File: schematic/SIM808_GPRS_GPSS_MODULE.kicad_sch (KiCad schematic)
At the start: 37 parts, among them IC4 SIM7600G-H_R2, J10 SIM_Card_Shielded, Q1 BC817, Q15 SI2302, Q16 SI2302, Q2 BC817

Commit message: Routing
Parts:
- removed J10: SIM_Card_Shielded, MACHADA_footprints:NANO_SIM_SHELL_SMN305, symbol fridgeduino-rescue:SIM_Card_Shielded-Connector-gsm_lora_logger-rescue-gsm_lora_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
- added J1: SIM7155-6-1-14-A, SIM7155-6-1-14-A_GCT, symbol simHolderPush:SIM7155-6-1-14-A
- AE3, AE4: footprint greencharge-footprints:UFL_COAX_CONN23370191 -> antenna:CONN_2337019-1_TEC
- IC4: footprint SIM7600GHR2 -> SIM7600:SIM7600GHR2
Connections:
- net GND: now also J1.C5 (GND), J1.CD, J1.GND1, J1.GND2, J1.GND3, J1.GND4, J1.GND5, J1.GND6
- net SIM_DATA: now also J1.C7 (I/O)
- net SIM_VDD: now also J1.C1 (VCC)
- net at D25.3 (TVS2), R88.1: now also J1.C2 (RST)
- net at D25.4 (TVS3), R89.1: now also J1.C3 (CLK)
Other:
- moved on the sheet: C74, C75, D25, D26, D27, Q1, Q15, Q16, Q2, R87, R88, R89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

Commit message: more Routing
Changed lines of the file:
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@@
 	(wire
 		(pts
-			(xy 200.66 66.04) (xy 204.47 66.04)
+			(xy 196.85 66.04) (xy 204.47 66.04)
 		)
 		(stroke

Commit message: changinge mcu and shift level
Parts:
- added C72, C73: 100n, Capacitor_SMD:C_0402_1005Metric, symbol Device:C_Small
- added IC1: RS0108YQ20, SOP65P640X120-20N, symbol rs0108yq20:RS0108YQ20
- added Q3, Q4, Q5, Q6, Q7: BC817, Package_TO_SOT_SMD:SOT-23, symbol Transistor_BJT:BC817
- added R100, R103, R104, R105, R106, R107, R108, R109: 4.7k, Resistor_SMD:R_0402_1005Metric, symbol Device:R_US
- added R110: 10k, Resistor_SMD:R_0402_1005Metric, symbol Device:R_US
- added R111, R112: 47k, Resistor_SMD:R_0402_1005Metric, symbol Device:R_US
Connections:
- net +3V3: now also C73.1, IC1.19 (VCCB), R105.1, R109.1
- net 1.8v_OUT: now also C72.1, IC1.2 (VCCA), Q5.1 (B), Q7.1 (B), R104.1, R107.1, R108.1, R110.1
- net DTR: now also IC1.6 (A5), Q4.3 (C), R107.2
- net GND: now also C72.2, C73.2, IC1.11 (GND), Q3.2 (E), Q4.2 (E), Q6.2 (E), R111.2, R112.2; no longer IC4.3 (PWRKEY)
- net LED_Status: now also IC1.7 (A6), Q7.2 (E)
- net SIM7600_RXD: now also IC1.4 (A3)
- net SIM7600_TXD: now also IC1.3 (A2)
- net Flight: now reaches IC4.54 (FLIGHTMODE)
- net Flight: now also IC1.5 (A4), Q3.3 (C)
- net RI: now reaches IC4.69 (RI)
- net RI: now also IC1.8 (A7), Q5.2 (E)
- new net: Q6.1 (B), R106.1
- new net: IC1.20 (B1), R112.1
- new net: Q3.1 (B), R100.2
- new net: Q4.1 (B), R103.2
- new net: IC1.1 (A1), R111.1
- new net: IC1.10 (OE), R110.2
- new net IO25: IC1.16 (B4)
- new net IO26: IC1.18 (B2)
- new net IO27: IC1.17 (B3)
- new net IO32: IC1.15 (B5)
- new net IO33: IC1.13 (B7)
- new net IO34: IC1.14 (B6)
- new net Sim_DTR_ESP: R103.1
- new net Sim_Flight_ESP: R100.1
- new net Sim_RI_esp: Q5.3 (C), R105.2
- new net Sim_Status_ESP: Q7.3 (C), R109.2
- new net Sim_pwkey_esp: R106.2
- new net pwrkey: IC4.3 (PWRKEY), Q6.3 (C), R104.2
- no-connect marks 79 -> 77

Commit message: changinge mcu and shift level
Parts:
- removed Q2, Q3, Q4, Q5, Q6, Q7: BC817, Package_TO_SOT_SMD:SOT-23, symbol Transistor_BJT:BC817
- removed R103, R104, R105, R106, R107, R108, R109, R87, R97, R98, R99: 4.7k, Resistor_SMD:R_0402_1005Metric, symbol Device:R_US
- added C76: 100n, Capacitor_SMD:C_0402_1005Metric, symbol fridgeduino-rescue:C_Small-Device
- added R101: 4.7k, Resistor_SMD:R_0402_1005Metric, symbol Device:R_US
- IC1: footprint SOP65P640X120-20N -> RS0108YQ20:SOP65P640X120-20N
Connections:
- net ESP_RX is gone; now on net GND: Q1.3 (C)
- net Sim_Flight_ESP is gone; now on an unnamed net: R100.1
- net GND: now also IC1.12 (B8), IC1.9 (A8), C76.1, R101.1
- net SIM7600_TXD: no longer Q1.2 (E)
- net pwrkey: now also Q1.2 (E), C76.2
- net IO4: now reaches R100.2
- net at Q1.1 (B): now also R101.2
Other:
- moved on the sheet: C72, C73, IC1, Q1, R110, R111, R112

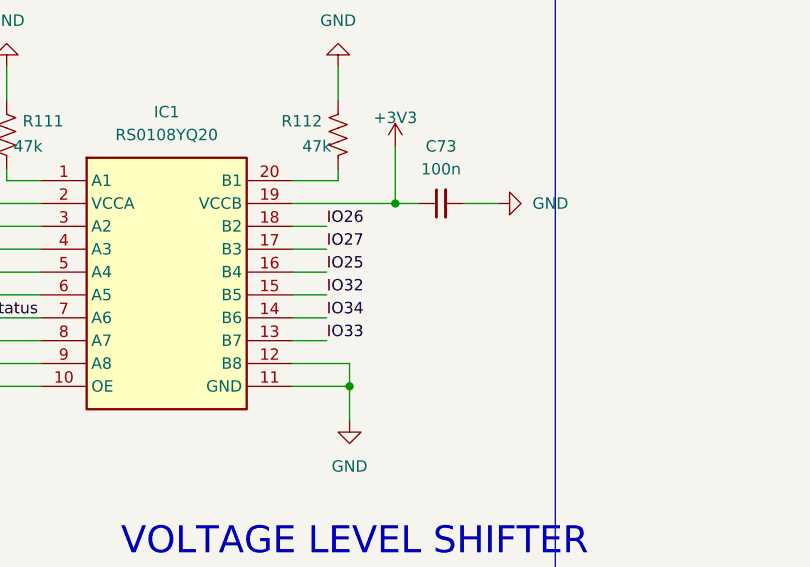
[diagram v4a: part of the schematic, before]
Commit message: MORE Routing with Global names
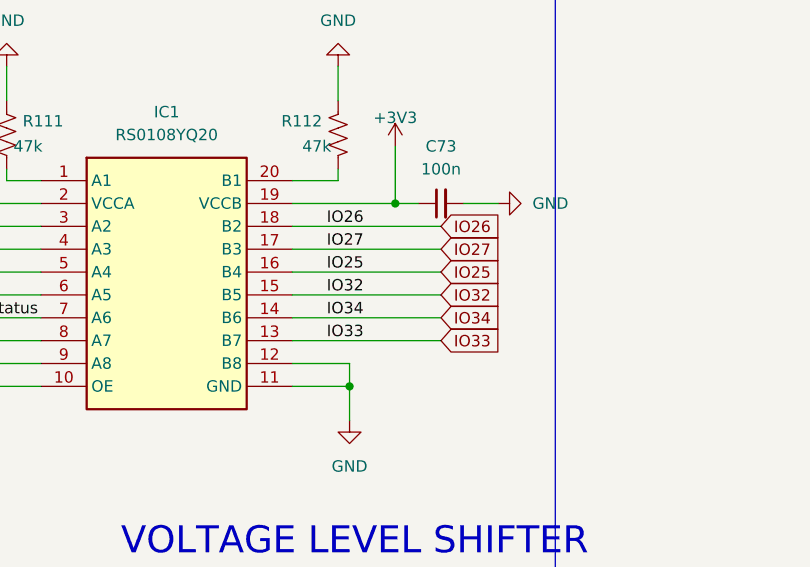
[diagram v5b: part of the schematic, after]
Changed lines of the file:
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@@
 	(wire
 		(pts
-			(xy 223.52 133.35) (xy 227.33 133.35)
+			(xy 223.52 133.35) (xy 240.03 133.35)
 		)
 		(stroke
@@
 	(wire
 		(pts
-			(xy 223.52 135.89) (xy 227.33 135.89)
+			(xy 223.52 135.89) (xy 240.03 135.89)
 		)
 		(stroke
@@
 	(wire
 		(pts
-			(xy 223.52 130.81) (xy 227.33 130.81)
+			(xy 223.52 130.81) (xy 240.03 130.81)
 		)
 		(stroke
@@
 	(wire
 		(pts
-			(xy 223.52 125.73) (xy 227.33 125.73)
+			(xy 223.52 125.73) (xy 240.03 125.73)
 		)
 		(stroke
@@
 	(wire
 		(pts
-			(xy 223.52 123.19) (xy 227.33 123.19)
+			(xy 223.52 123.19) (xy 240.03 123.19)
 		)
 		(stroke
@@
 	(wire
 		(pts
-			(xy 223.52 128.27) (xy 227.33 128.27)
+			(xy 223.52 128.27) (xy 240.03 128.27)
 		)
 		(stroke
@@
 			)
 			(justify left bottom)
+		)
+	)
+	(global_label "IO34"
+		(shape input)
+		(at 240.03 133.35 0)
+		(fields_autoplaced yes)
+		(effects
+			(font
+				(size 1.27 1.27)
+			)
+			(justify left)
+		)
+		(property "Intersheetrefs" "${INTERSHEET_REFS}"
+			(at 247.3695 133.35 0)
+			(effects
+				(font
+					(size 1.27 1.27)
+				)
+				(justify left)
+				(hide yes)
+			)
+		)
+	)
+	(global_label "IO26"
+		(shape input)
+		(at 240.03 123.19 0)
+		(fields_autoplaced yes)
+		(effects
+			(font
+				(size 1.27 1.27)
+			)
+			(justify left)
+		)
+		(property "Intersheetrefs" "${INTERSHEET_REFS}"
+			(at 247.3695 123.19 0)
+			(effects
+				(font
+					(size 1.27 1.27)
+				)
+				(justify left)
+				(hide yes)
+			)
 		)
 	)
@@
 		)
 	)
+	(global_label "IO33"
+		(shape input)
+		(at 240.03 135.89 0)
+		(fields_autoplaced yes)
+		(effects
+			(font
+				(size 1.27 1.27)
+			)
+			(justify left)
+		)
+		(property "Intersheetrefs" "${INTERSHEET_REFS}"
+			(at 247.3695 135.89 0)
+			(effects
+				(font
+					(size 1.27 1.27)
+				)
+				(justify left)
+				(hide yes)
+			)
+		)
+	)
+	(global_label "IO27"
+		(shape input)
+		(at 240.03 125.73 0)
+		(fields_autoplaced yes)
+		(effects
+			(font
+				(size 1.27 1.27)
+			)
+			(justify left)
+		)
+		(property "Intersheetrefs" "${INTERSHEET_REFS}"
+			(at 247.3695 125.73 0)
+			(effects
+				(font
+					(size 1.27 1.27)
+				)
+				(justify left)
+				(hide yes)
+			)
+		)
+	)
 	(global_label "4.2v"
 		(shape input)
@@
 				(hide yes)
 			)
+		)
+	)
+	(global_label "IO32"
+		(shape input)
+		(at 240.03 130.81 0)
+		(fields_autoplaced yes)
+		(effects
+			(font
+				(size 1.27 1.27)
+			)
+			(justify left)
+		)
+		(property "Intersheetrefs" "${INTERSHEET_REFS}"
+			(at 247.3695 130.81 0)
+			(effects
+				(font
+					(size 1.27 1.27)
+				)
+				(justify left)
+				(hide yes)
+			)
+		)
+	)
+	(global_label "IO25"
+		(shape input)
+		(at 240.03 128.27 0)
+		(fields_autoplaced yes)
+		(effects
+			(font
+				(size 1.27 1.27)
+			)
+			(justify left)
+		)
+		(property "Intersheetrefs" "${INTERSHEET_REFS}"
+			(at 247.3695 128.27 0)
+			(effects
+				(font
+					(size 1.27 1.27)
+				)
+				(justify left)
+				(hide yes)
+			)
